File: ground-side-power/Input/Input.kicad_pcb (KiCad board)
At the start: 2 copper layers, 100.3 x 130 mm, 41 parts, among them J1 Battery Terminals, J2 Battery Terminals, J26 Conn_01x02_Female, J3 Battery Terminals, J4 Battery Terminals, J5 455860005, J6 455860005, J7 ATX-24, J8 Conn_01x03_Female, J9 Conn_01x03_Female, K1 AZ2150_AMZ, M1 Fan_PC_Chassis, SW1 GRB234A2NABA1, U1 INA180, U2 INA180

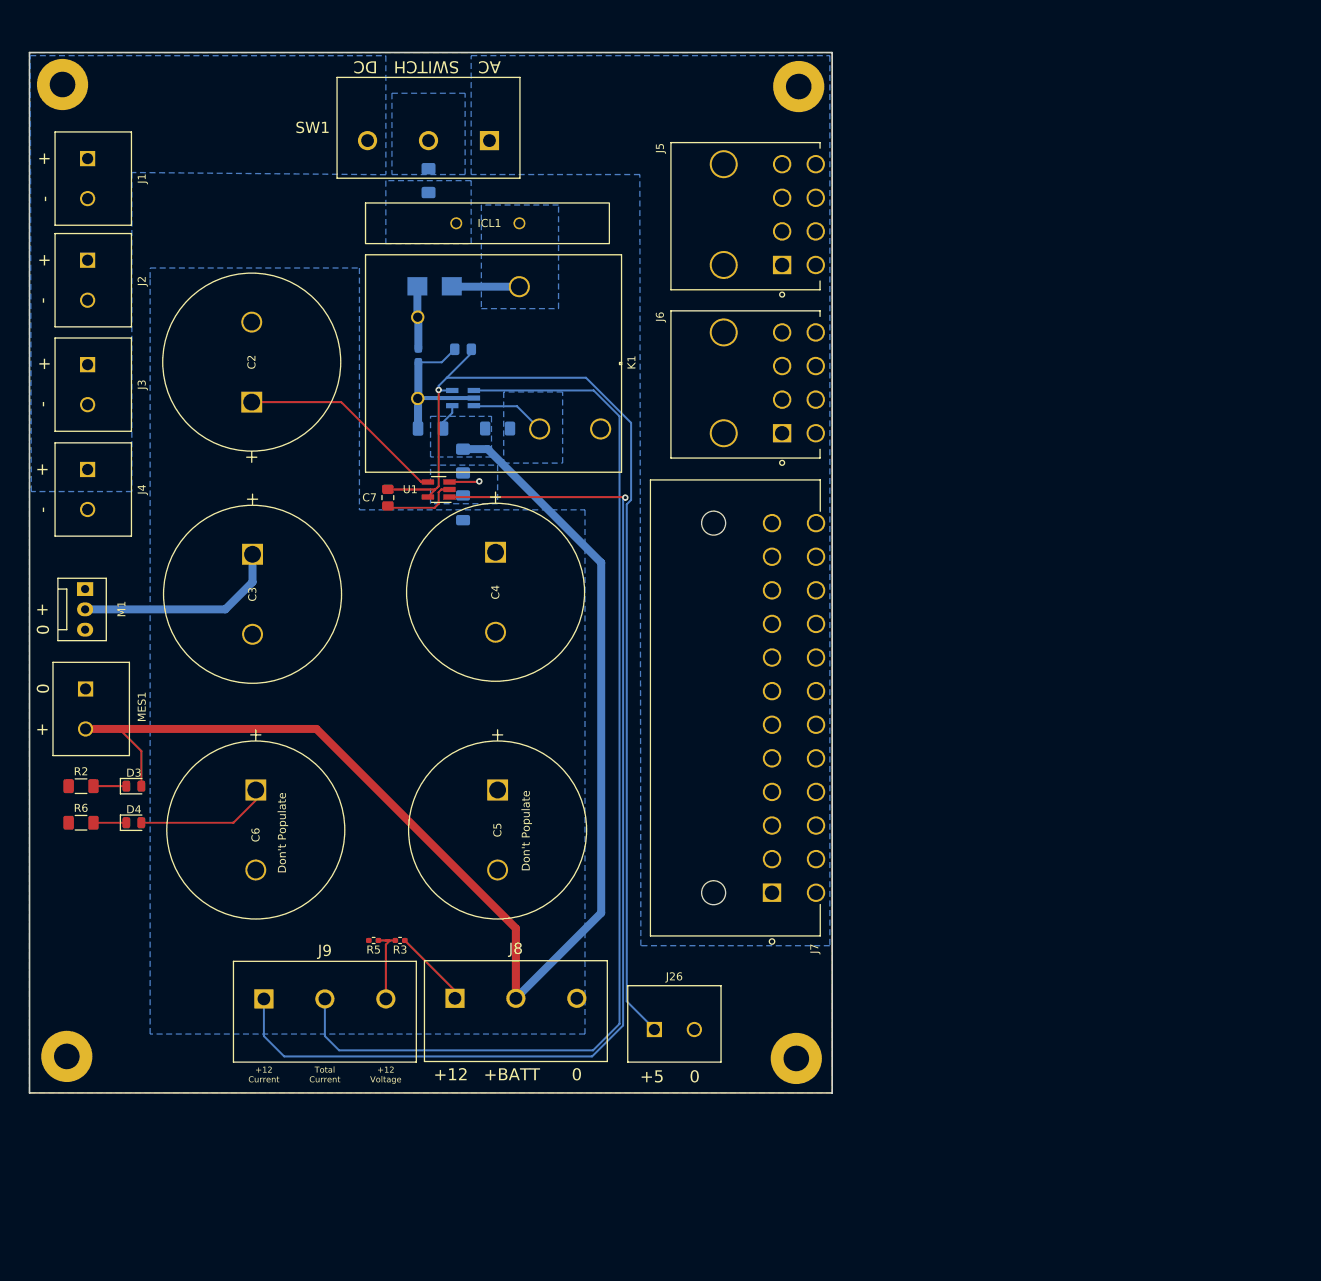
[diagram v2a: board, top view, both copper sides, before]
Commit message: Address Input and Converter Comments
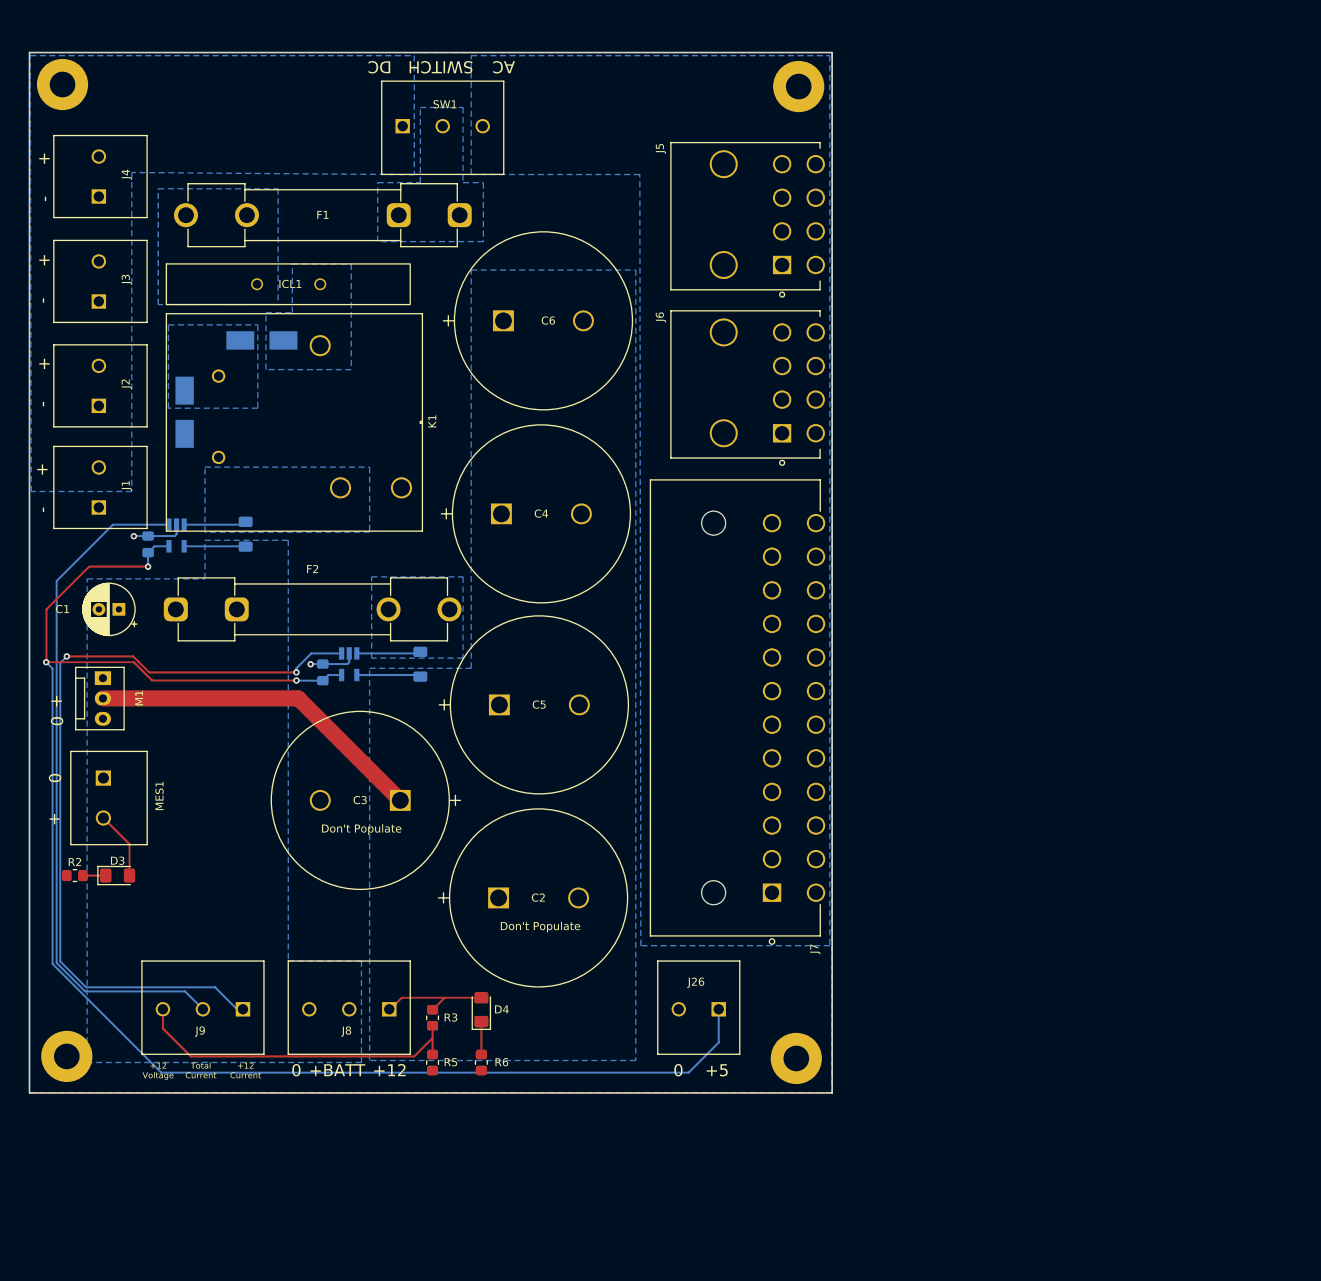
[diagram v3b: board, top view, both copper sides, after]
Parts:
- C1: footprint Capacitor_SMD:C_1206_3216Metric_Pad1.33x1.80mm_HandSolder -> Capacitor_THT:CP_Radial_D6.3mm_P2.50mm; moved to F.Cu
- C7, U1: moved to B.Cu
- D1: footprint Capacitor_SMD:C_0603_1608Metric_Pad1.08x0.95mm_HandSolder -> Diode_SMD:D_SMB_Handsoldering
- D2: footprint Diode_SMD:D_SMB -> Diode_SMD:D_SMB_Handsoldering
- D3, D4: footprint Diode_SMD:D_0805_2012Metric -> Diode_SMD:D_1206_3216Metric_Pad1.42x1.75mm_HandSolder
- F1, F2: footprint Fuse:Fuse_1206_3216Metric_Pad1.42x1.75mm_HandSolder -> Fuse:Fuseholder_Clip-6.3x32mm_Littelfuse_102_122_Inline_P34.21x7.62mm_D1.98mm_Horizontal; moved to F.Cu
- J1, J2, J26, J3, J4: footprint GSP:OSTTA020161 -> GSP:1935310
- J8, J9, SW1: footprint GSP:TB005-762-03BE -> GSP:1935323
- K1: value AZ2150_AMZ -> AZ2150-1A-12DEF
- R2, R6: footprint Resistor_SMD:R_1206_3216Metric_Pad1.30x1.75mm_HandSolder -> Resistor_SMD:R_0805_2012Metric_Pad1.20x1.40mm_HandSolder
- R3, R5: footprint Resistor_SMD:R_0402_1005Metric_Pad0.72x0.64mm_HandSolder -> Resistor_SMD:R_0805_2012Metric_Pad1.20x1.40mm_HandSolder
- moved C2 69.2 mm to (99.2, 138.2), turned to 0 degrees
- moved C6 66.3 mm to (99.8, 66.0), turned to 0 degrees
- moved R6 58.3 mm to (97.0, 158.8), turned to 90 degrees
- moved D4 49.3 mm to (97.0, 152.1), turned to 90 degrees
- moved C8 46.3 mm to (55.4, 94.0), turned to -90 degrees
- moved C1 45.0 mm to (51.7, 102.1)
- moved J1 43.6 mm to (49.2, 89.4), turned to 90 degrees
- moved F2 40.4 mm to (58.8, 102.1), turned to 0 degrees
- moved U2 39.7 mm to (58.9, 92.9), turned to -90 degrees
- moved C3 35.9 mm to (86.9, 126.0), turned to 180 degrees
- moved R1 34.2 mm to (67.6, 92.7), turned to -90 degrees
- moved J4 34.1 mm to (49.2, 50.5), turned to 90 degrees
- moved D1 30.1 mm to (59.9, 77.5)
- moved ICL1 26.0 mm to (72.9, 61.5)
- moved K1 26.0 mm to (64.2, 83.1)
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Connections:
- SW1 pad 1: /ACPowerSupply -> /BatteryPowerSupply
- SW1 pad 3: /BatteryPowerSupply -> /ACPowerSupply
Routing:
- net +BATT: track 166.0 -> 16.4 mm
- net +5V: track 129.3 -> 197.1 mm, vias 1 -> 3
- net /TOTAL_OUT: track 139.1 -> 85.4 mm
- net /12V_OUT: track 140.3 -> 100.2 mm, vias 1 -> 2
- net /12_VOLTAGE: track 10.1 -> 42.1 mm
- net GND: track 30.2 -> 12.7 mm, vias 0 -> 2
- net +12V: track 77.3 -> 64.7 mm
- net Net-(D2-Pad2): track 8.46 -> 0.00 mm
- net Net-(D1-Pad1): track 7.82 -> 0.00 mm
- net /12V_Sense+: track 3.76 -> 8.02 mm, vias 1 -> 0
- net /Sys_Sense+: track 9.33 -> 7.72 mm
- net Net-(D3-Pad1): track 4.12 -> 2.85 mm
- added copper zone on B.Cu, net Net-(D1-Pad1)

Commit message: Resolved Final Issues
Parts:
- removed C5, C6: 22mF, GSP:LLS1C223MELZ
- added G***: LOGO, rlcs:rocketry_logo_small, F.Cu at (119.5, 46.1)
- added R17: 10k, Resistor_SMD:R_0805_2012Metric_Pad1.20x1.40mm_HandSolder, F.Cu at (165.1, 58.1)
- J5, J6: value 455860005 -> 874270842; footprint GSP:MOLEX_455860005 -> GSP:MOLEX_874270842
- J7: footprint GSP:MOLEX_15246240 -> GSP:MOLEX_442060001
- R1, R4: value 0.0016 -> 0.0015; footprint Resistor_SMD:R_1206_3216Metric_Pad1.30x1.75mm_HandSolder -> Resistor_SMD:R_2512_6332Metric_Pad1.40x3.35mm_HandSolder
- moved C3 90.5 mm to (159.7, 72.3), turned to 0 degrees
- moved C2 62.7 mm to (159.2, 120.3)
- moved J9 61.7 mm to (128.5, 144.6)
- moved J8 61.7 mm to (146.7, 144.6)
- moved C4 60.3 mm to (159.5, 96.4)
- moved ? 59.1 mm to (195.3, 153.8)
- moved ? 58.9 mm to (195.3, 42.4)
- moved M1 58.6 mm to (107.9, 117.7)
- moved ICL1 58.5 mm to (131.1, 67.7)
- moved C1 58.5 mm to (109.9, 108.3)
- moved J1 58.5 mm to (107.4, 95.6)
- moved J2 58.5 mm to (107.4, 82.9)
- moved J3 58.5 mm to (107.4, 69.8)
- moved J4 58.5 mm to (107.4, 56.7)
- moved C7 58.5 mm to (135.4, 116.2)
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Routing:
- net +5V: track 197.1 -> 165.1 mm
- net +12V: track 64.7 -> 85.6 mm
- net /12_VOLTAGE: track 42.1 -> 31.1 mm
- net /12V_OUT: track 100.2 -> 89.7 mm
- net /TOTAL_OUT: track 85.4 -> 78.0 mm
- net GND: track 12.7 -> 19.2 mm
- net /Sys_Sense+: track 7.72 -> 9.41 mm
- net +BATT: track 16.4 -> 17.6 mm
- net /12V_Sense+: track 8.02 -> 8.64 mm
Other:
- board size 100.3 x 130 mm -> 102 x 119.7 mm
- board text added: "Ground Side Power Input Board Domenic Hampson Elias Kountouris"

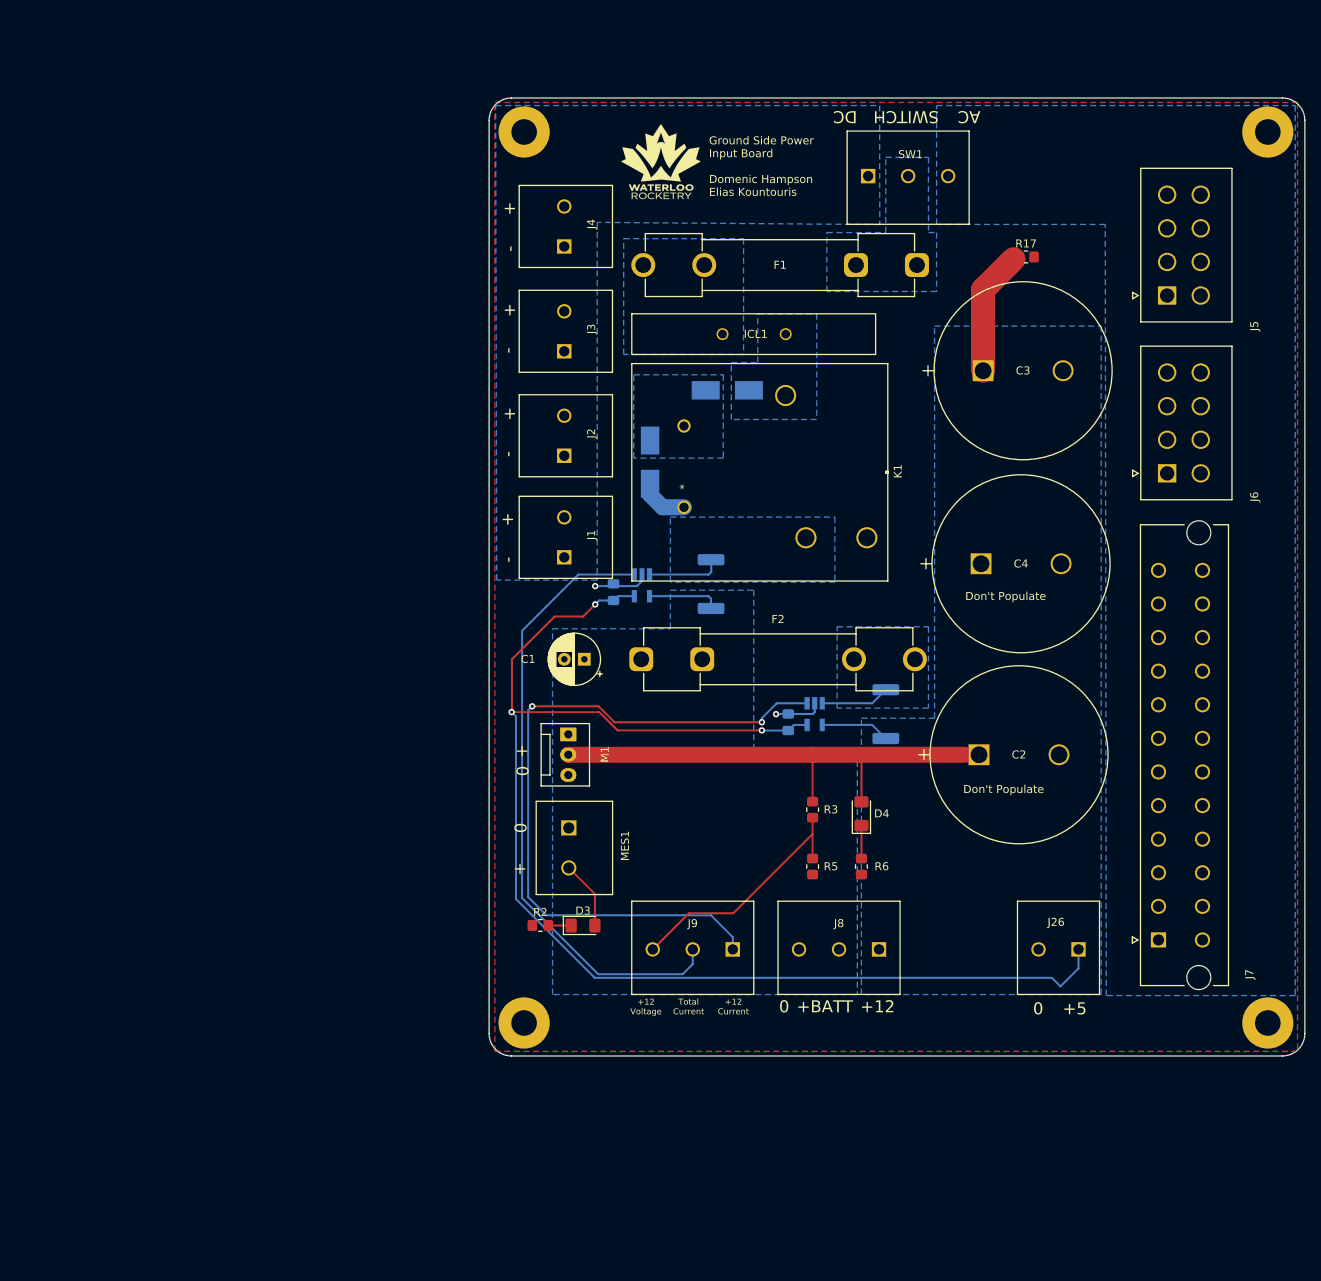
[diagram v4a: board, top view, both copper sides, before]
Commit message: Silkscreen and current sense changes
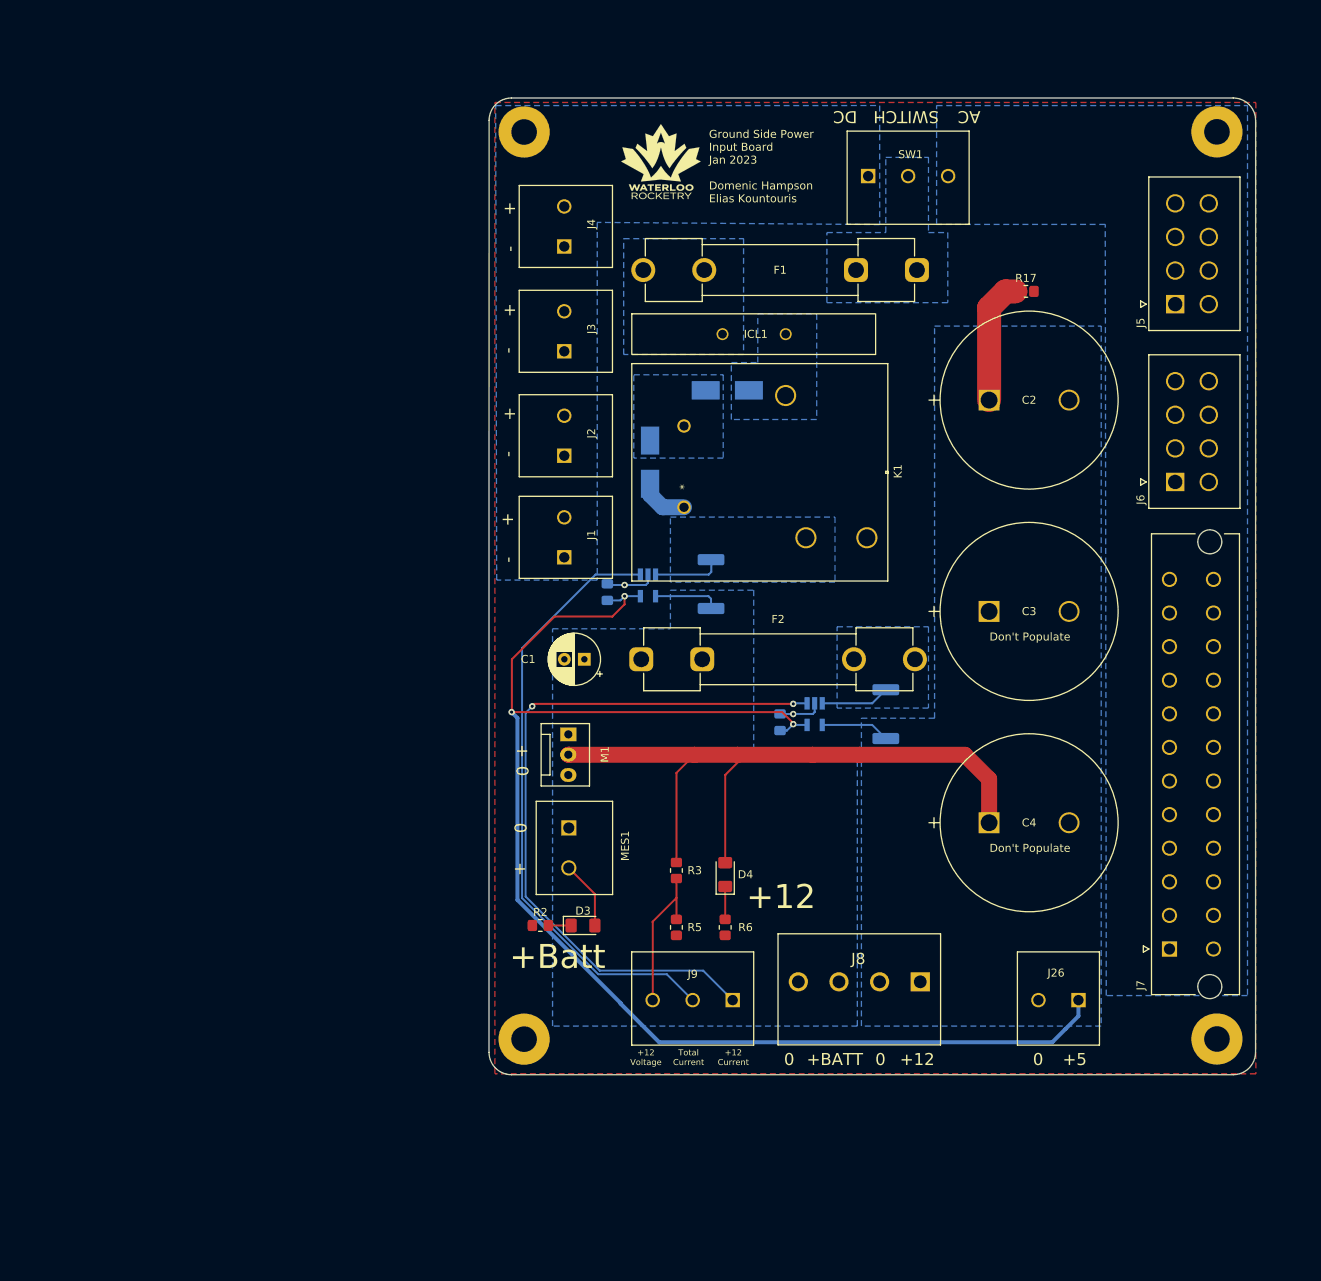
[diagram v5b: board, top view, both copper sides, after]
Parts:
- J8: footprint GSP:1935323 -> GSP:CUI_TB008A-508-04BE
- moved C2 44.4 mm to (160.5, 75.9)
- moved C4 32.4 mm to (160.5, 128.8)
- moved C3 30.1 mm to (160.5, 102.4)
- moved D4 18.6 mm to (127.5, 135.3)
- moved R6 18.6 mm to (127.5, 141.9)
- moved R3 18.6 mm to (121.4, 134.7)
- moved R5 18.6 mm to (121.4, 141.9)
- moved ? 6.67 mm to (189.0, 155.8)
- moved J8 6.55 mm to (151.9, 148.7)
- moved ? 6.36 mm to (189.0, 42.4)
- moved J26 6.34 mm to (171.7, 150.9)
- moved J9 6.34 mm to (128.4, 150.9)
- moved R17 4.31 mm to (165.1, 62.4)
- moved ? 2.02 mm to (102.4, 155.8)
- moved J7 1.78 mm to (183.0, 144.6)
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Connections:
- J8 pad 2: +BATT -> GND
- J8 pad 3: GND -> +BATT
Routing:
- net +12V: track 85.6 -> 112.6 mm
- net /12_VOLTAGE: track 31.1 -> 19.1 mm
- net +5V: track 165.1 -> 173.2 mm
- net GND: track 19.2 -> 17.4 mm
- net /TOTAL_OUT: track 78.0 -> 76.5 mm
- net /Sys_Sense+: track 9.41 -> 8.66 mm
- net +BATT: track 17.6 -> 16.8 mm
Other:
- board size 102 x 119.7 mm -> 95.8 x 122.1 mm
- board text added: "+Batt"
- board text added: "Ground Side Power Input Board Jan 2023 Domenic Hampson Elias Kountouris"
- board text removed: "Ground Side Power Input Board Domenic Hampson Elias Kountouris"
